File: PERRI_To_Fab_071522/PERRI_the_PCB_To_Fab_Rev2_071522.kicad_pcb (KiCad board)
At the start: 2 copper layers, 163 x 100 mm, 45 parts, among them J1 SS5-80-3.00-X-D-K-XX, J2 External power, J3 Conn_02x50_Counter_Clockwise, J4 Conn_02x05_Counter_Clockwise, J5 SS5-80-3.00-X-D-K-XX, J6 Conn_01x03, J7 Conn_01x03, J8 Conn_01x03, SW2 SW_DIP_x08, U1 TMP441AIDCNR, U2 TPS2595, U3 PCA9554ADB, U4 NCV8508

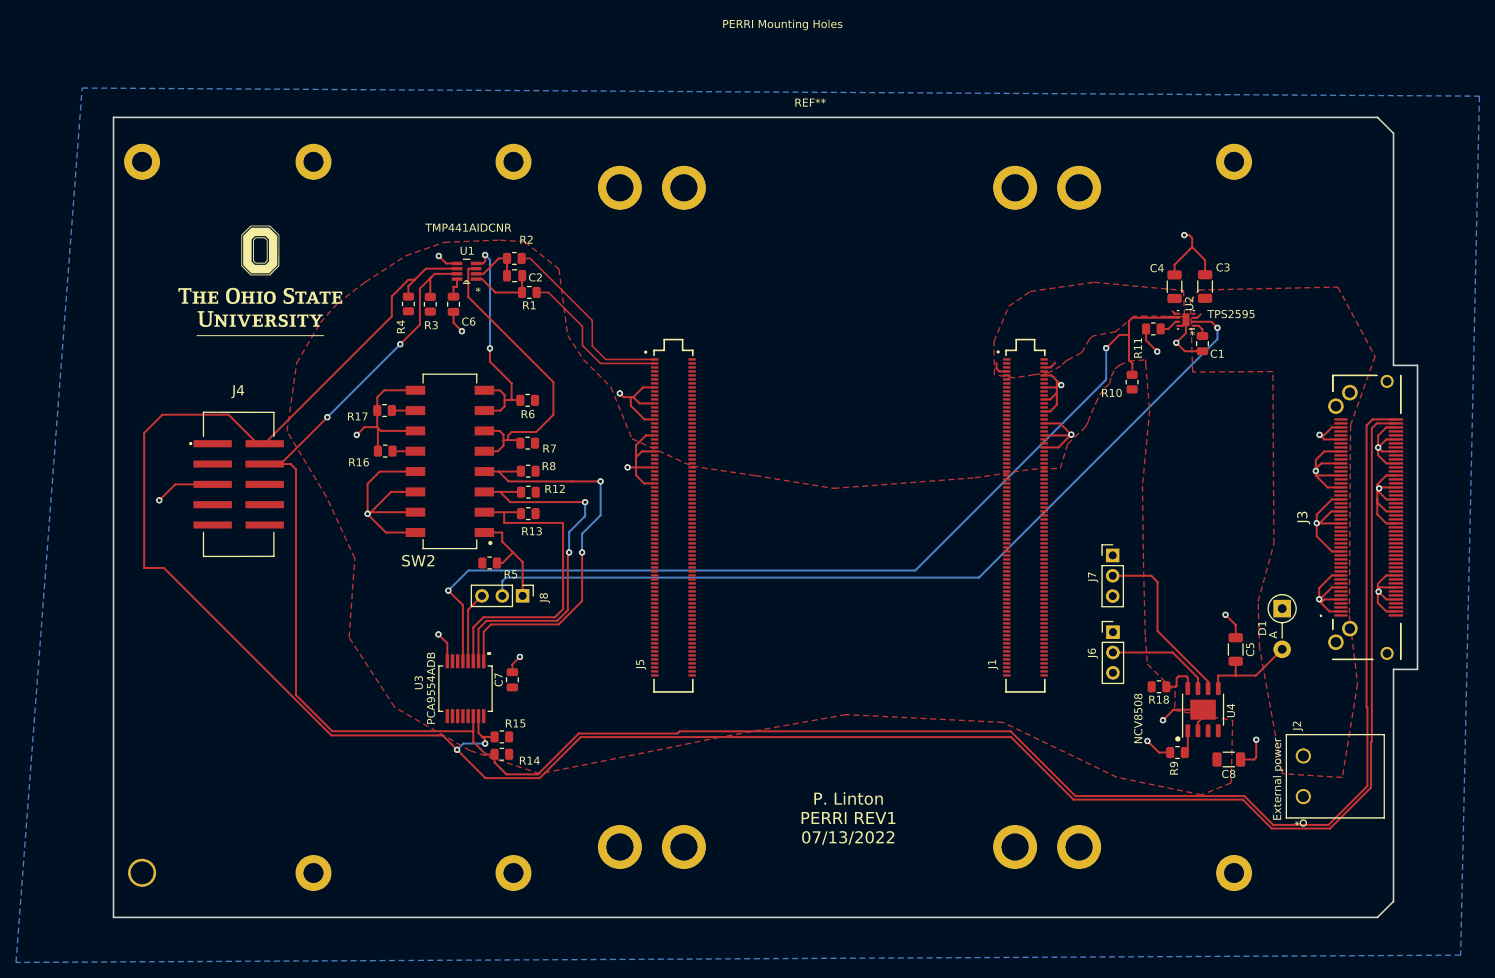
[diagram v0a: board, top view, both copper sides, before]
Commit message: changed 2x5 connector on PERRI
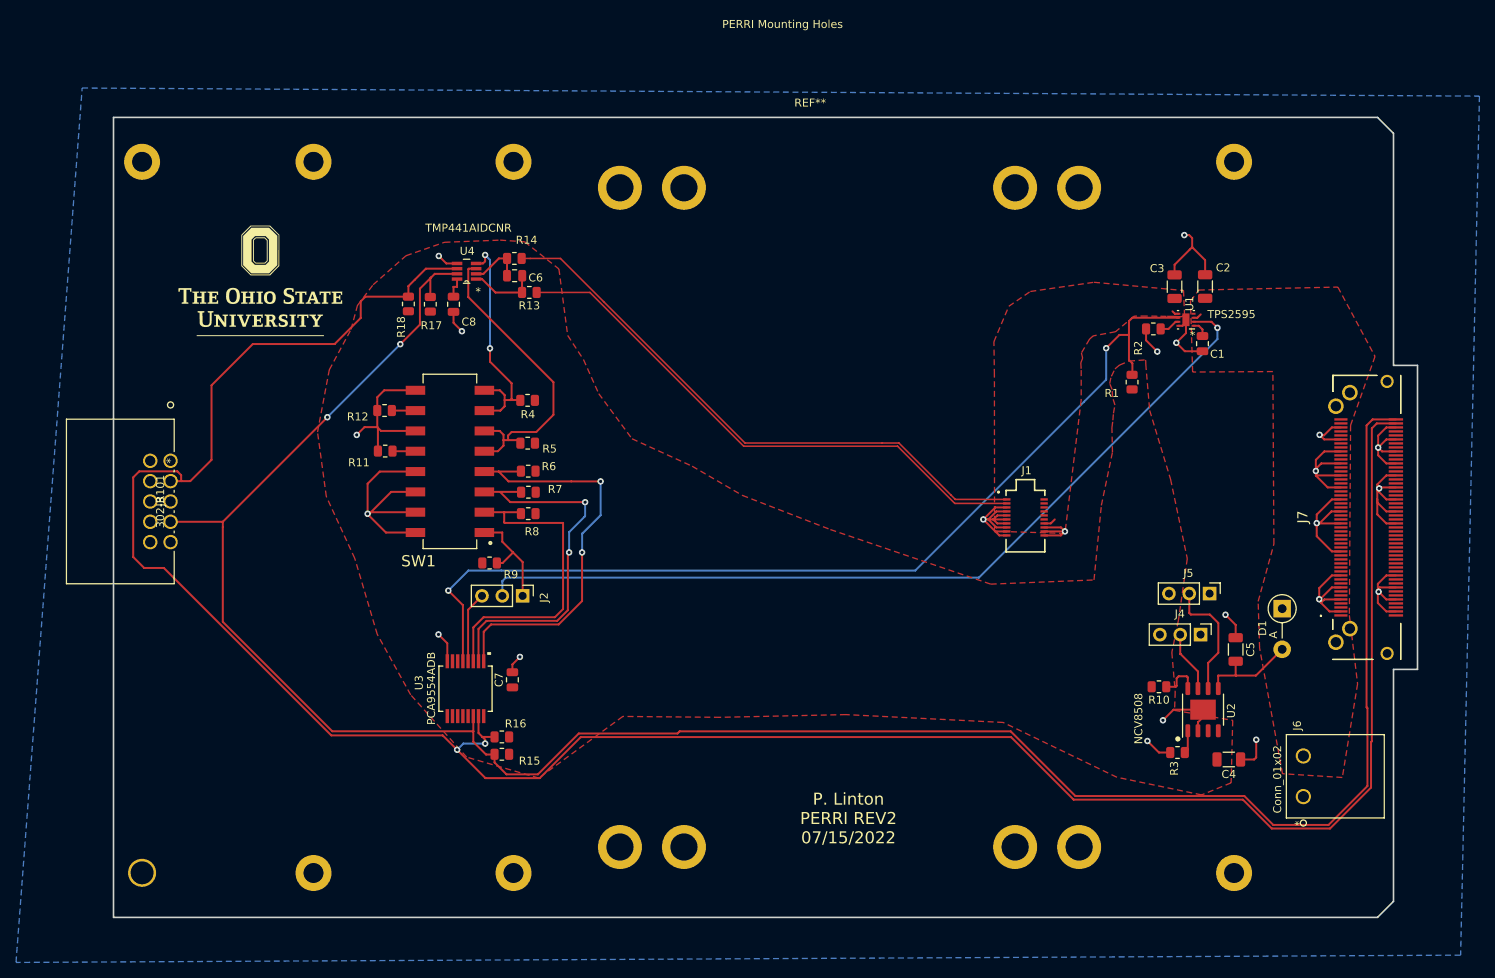
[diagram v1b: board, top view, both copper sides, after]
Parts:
- removed the J4 at (103.8, 92.1)
- removed the J5 at (158.4, 96.2)
- added J3: 302-R101, footprints:302-R101, F.Cu at (95.5, 89.2)
- J1: value SS5-80-3.00-X-D-K-XX -> SS5-10-3.00-X-D-K-XX; footprint footprints:SAMTEC_SS5-80-3.00-X-D-K-XX -> footprints:SAMTEC_SS5-10-3.00-X-D-K-XX
- J6: renamed from J2; value External power -> Conn_01x02
- moved J5 13.0 mm to (225.4, 105.8), turned to -90 degrees
- moved J4 11.0 mm to (224.3, 110.9), turned to -90 degrees
- renumbered C3 to C2, C4 to C3, C8 to C4, C2 to C6, C6 to C8, J8 to J2, J6 to J4, J7 to J5, J3 to J7, R10 to R1, R18 to R10, R16 to R11, R17 to R12, R1 to R13, R2 to R14, R14 to R15, R15 to R16, R3 to R17, R4 to R18, R11 to R2, R9 to R3, R6 to R4, R7 to R5, R8 to R6, R12 to R7, R13 to R8, R5 to R9, SW2 to SW1, U2 to U1, U4 to U2, U1 to U4
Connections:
- J1 pad 01: /12V_To_Hat -> /DXN
- J1 pad 03: /12V_To_Hat -> /DXP
- J1 pad 05: /12V_To_Hat -> GND
- J1 pad 07: /12V_To_Hat -> GND
- J1 pad 08: unconnected-(J1-Pad08) -> /12V_To_Hat
- J1 pad 09: unconnected-(J1-Pad09) -> GND
- J1 pad 10: GND -> /12V_To_Hat
- J1 pad 11: unconnected-(J1-Pad11) -> GND
- J1 pad 12: unconnected-(J1-Pad12) -> /12V_To_Hat
- J1 pad 13: unconnected-(J1-Pad13) -> GND
- J1 pad 14: unconnected-(J1-Pad14) -> /12V_To_Hat
- J1 pad 15: unconnected-(J1-Pad15) -> GND
- J1 pad 17: unconnected-(J1-Pad17) -> GND
- J1 pad 18: unconnected-(J1-Pad18) -> GND
- J1 pad 19: unconnected-(J1-Pad19) -> GND
- J1 pad 20: unconnected-(J1-Pad20) -> GND
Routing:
- net /DXP: track 19.8 -> 69.7 mm
- net /DXN: track 23.7 -> 73.1 mm
- net GND: track 257.3 -> 230.2 mm, vias 25 -> 22
- net /SCL: track 270.9 -> 278.7 mm
- net Net-(J5-Pad2): track 21.9 -> 15.3 mm
- net Net-(J4-Pad2): track 13.3 -> 7.67 mm
- net /12V_To_Hat: track 4.62 -> 2.41 mm
- net /SDA: track 302.0 -> 304.0 mm
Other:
- board text added: "P. Linton PERRI REV2 07/15/2022"
- board text removed: "P. Linton PERRI REV1 07/13/2022"
